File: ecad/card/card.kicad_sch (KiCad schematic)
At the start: 133 parts, among them J1 Conn_01x03_Pin, J2 USB4105-GF-A, J3 10145226-0241N13LF, SW1 SW_Push, SW2 SW_Push, U1 W25Q128JVS, U2 RP2350_80QFN, U3 MCP23017_SO, U4 NCP1117-3.3_SOT223, U5 MCP23017_SO, X1 ABM8-272-T3

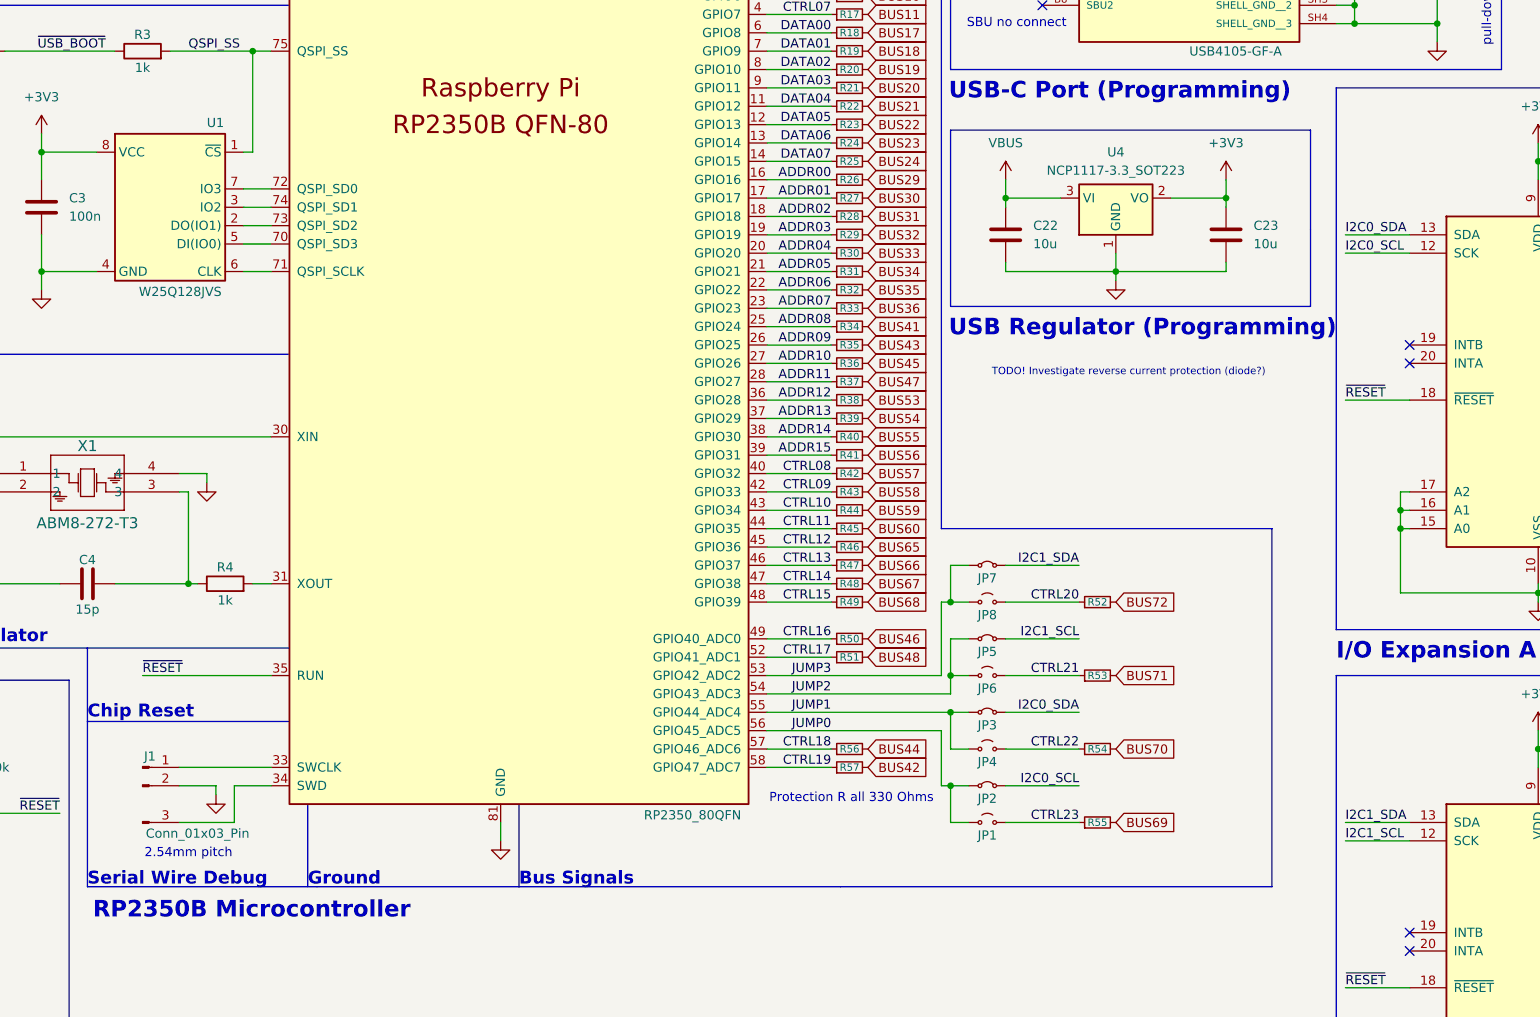
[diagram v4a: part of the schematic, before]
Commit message: card add UART output, protection diode
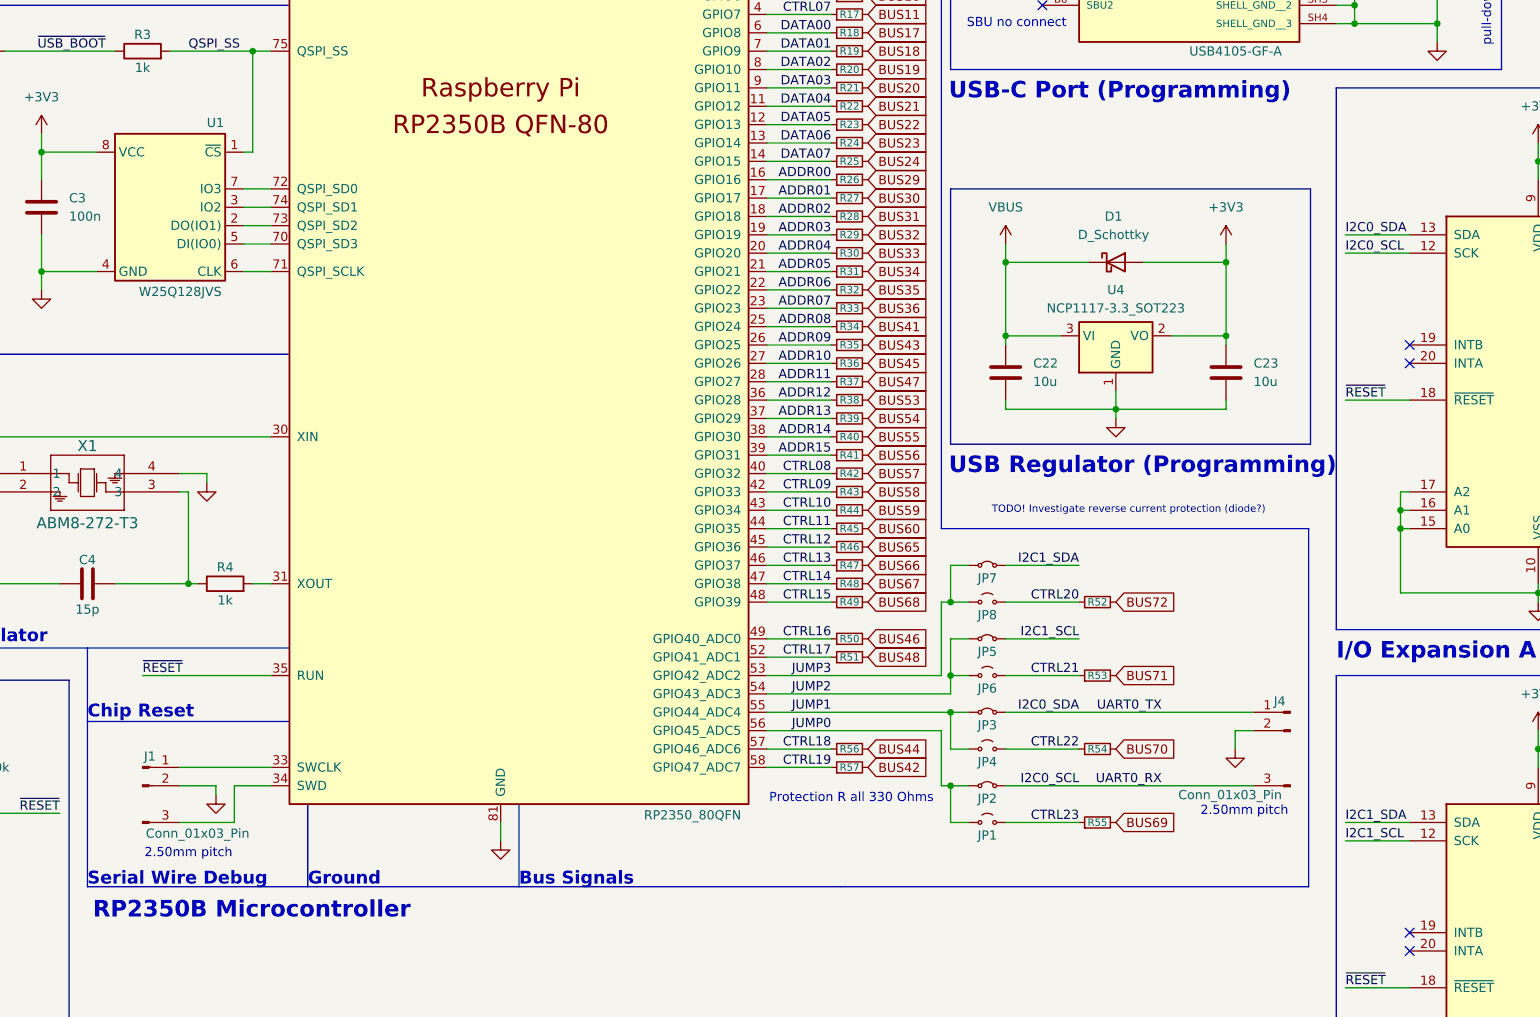
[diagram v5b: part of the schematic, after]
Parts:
- added D1: D_Schottky, Diode_SMD:D_0402_1005Metric, symbol Device:D_Schottky
- added J4: Conn_01x03_Pin, Connector_JST:JST_XH_B3B-XH-AM_1x03_P2.50mm_Vertical, symbol Connector:Conn_01x03_Pin
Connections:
- net +3V3: now also D1.2 (A)
- net GND: now also J4.2 (Pin_2)
- net I2C0_SCL: now also J4.3 (Pin_3)
- net I2C0_SDA: now also J4.1 (Pin_1)
- net VBUS: now also D1.1 (K)
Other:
- note added: "2.50mm pitch"
- note removed: "2.54mm pitch"
- moved on the sheet: C22, C23, U4

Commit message: Finished Card and Panel Schematics
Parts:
- added D2: Debugging, Diode_SMD:D_0402_1005Metric_Pad0.77x0.64mm_HandSolder, symbol Device:D
- added D3: Protection, Diode_SMD:D_0402_1005Metric_Pad0.77x0.64mm_HandSolder, symbol Device:D_Schottky
- D1: footprint Diode_SMD:D_0402_1005Metric -> Diode_SMD:D_0402_1005Metric_Pad0.77x0.64mm_HandSolder
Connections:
- net GND: now also D2.1 (K), D3.2 (A)
- net VBUS: now also D2.2 (A)
- net +3V3 renamed 3.3V
- net 3.3V: now also D3.1 (K)
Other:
- note added: "*Not used in PCB"
- note added: "PWR FLAGS"
